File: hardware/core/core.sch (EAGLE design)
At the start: 710 parts, among them IC1 MAX481CSA, IC10 MAX481CSA, IC11 MAX481CSA, IC12 MAX481CSA, IC13 MAX481CSA, IC14 MAX481CSA, IC15 MAX481CSA, IC16 MAX481CSA, IC17 MAX481CSA, IC18 MAX481CSA, IC19 MAX481CSA, IC2 LD117AS12TR, IC20 MAX481CSA, IC21 MAX481CSA, IC22 LD117AS12TR, IC3 MAX481CSA, IC4 MAX481CSA, IC5 MAX481CSA, IC6 MAX481CSA, IC7 MAX481CSA, IC8 MAX481CSA, IC9 MAX481CSA, U1 6N138SDM

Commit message: v04 complete
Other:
- note added: "MIDI-IN Interface"
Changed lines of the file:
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@@
 <wire x1="1366.52" y1="0" x2="1366.52" y2="408.94" width="0.1524" layer="98"/>
 <wire x1="1366.52" y1="408.94" x2="254" y2="408.94" width="0.1524" layer="98"/>
+<text x="5.08" y="393.7" size="2.54" layer="98">MIDI-IN Interface</text>
 </plain>
 <instances>

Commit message: updates
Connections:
- removed net N$84: D1.C, D50.C, D51.C, D52.C, D53.C, D54.C, D55.C, D56.C
- net GND: now also D1.C, D50.C, D51.C, D52.C, D53.C, D54.C, D55.C, D56.C
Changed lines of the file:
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@@
 </part>
 <part name="GND49" library="supply1" library_urn="urn:adsk.eagle:library:371" deviceset="GND" device=""/>
-<part name="GND122" library="supply1" library_urn="urn:adsk.eagle:library:371" deviceset="GND" device=""/>
 <part name="D171" library="SMBJ8.0CA" library_urn="urn:adsk.eagle:library:39221370" deviceset="SMBJ8.0CA" device="" package3d_urn="urn:adsk.eagle:package:39221373/1">
 <attribute name="DESCRIPTION" value="600 Watt TVS 5.0v working, 9v clamp"/>
@@
 <part name="GND108" library="supply1" library_urn="urn:adsk.eagle:library:371" deviceset="GND" device=""/>
 <part name="J1" library="SparkFun-Connectors" library_urn="urn:adsk.eagle:library:513" deviceset="CONN_05X2" device="SHD" package3d_urn="urn:adsk.eagle:package:38000/1"/>
+<part name="GND122" library="supply1" library_urn="urn:adsk.eagle:library:371" deviceset="GND" device=""/>
 </parts>
 <sheets>
@@
 <attribute name="VALUE" x="949.96" y="279.4" size="1.778" layer="96"/>
 </instance>
-<instance part="GND122" gate="1" x="995.68" y="284.48" smashed="yes">
-<attribute name="VALUE" x="993.14" y="281.94" size="1.778" layer="96"/>
-</instance>
 <instance part="D171" gate="G$1" x="363.22" y="88.9" smashed="yes" rot="R90">
 <attribute name="NAME" x="363.22" y="96.52" size="1.778" layer="95" rot="R90"/>
@@
 <attribute name="NAME" x="151.13" y="122.428" size="1.778" layer="95" font="vector"/>
 </instance>
+<instance part="GND122" gate="1" x="995.68" y="281.94" smashed="yes">
+<attribute name="VALUE" x="993.14" y="279.4" size="1.778" layer="96"/>
+</instance>
 </instances>
 <busses>
@@
 <label x="165.1" y="109.22" size="1.778" layer="95"/>
 </segment>
+<segment>
+<pinref part="D56" gate="G$1" pin="C"/>
+<wire x1="995.68" y1="386.08" x2="995.68" y2="378.46" width="0.1524" layer="91"/>
+<wire x1="995.68" y1="378.46" x2="995.68" y2="370.84" width="0.1524" layer="91"/>
+<wire x1="995.68" y1="370.84" x2="995.68" y2="363.22" width="0.1524" layer="91"/>
+<wire x1="995.68" y1="363.22" x2="995.68" y2="314.96" width="0.1524" layer="91"/>
+<wire x1="995.68" y1="314.96" x2="995.68" y2="307.34" width="0.1524" layer="91"/>
+<wire x1="995.68" y1="307.34" x2="995.68" y2="299.72" width="0.1524" layer="91"/>
+<wire x1="995.68" y1="299.72" x2="995.68" y2="292.1" width="0.1524" layer="91"/>
+<wire x1="993.14" y1="292.1" x2="995.68" y2="292.1" width="0.1524" layer="91"/>
+<wire x1="995.68" y1="292.1" x2="995.68" y2="284.48" width="0.1524" layer="91"/>
+<pinref part="D55" gate="G$1" pin="C"/>
+<wire x1="993.14" y1="299.72" x2="995.68" y2="299.72" width="0.1524" layer="91"/>
+<junction x="995.68" y="299.72"/>
+<pinref part="D54" gate="G$1" pin="C"/>
+<wire x1="993.14" y1="307.34" x2="995.68" y2="307.34" width="0.1524" layer="91"/>
+<junction x="995.68" y="307.34"/>
+<pinref part="D53" gate="G$1" pin="C"/>
+<wire x1="993.14" y1="314.96" x2="995.68" y2="314.96" width="0.1524" layer="91"/>
+<junction x="995.68" y="314.96"/>
+<pinref part="D1" gate="G$1" pin="C"/>
+<wire x1="993.14" y1="386.08" x2="995.68" y2="386.08" width="0.1524" layer="91"/>
+<pinref part="D50" gate="G$1" pin="C"/>
+<wire x1="993.14" y1="378.46" x2="995.68" y2="378.46" width="0.1524" layer="91"/>
+<junction x="995.68" y="378.46"/>
+<pinref part="D51" gate="G$1" pin="C"/>
+<wire x1="993.14" y1="370.84" x2="995.68" y2="370.84" width="0.1524" layer="91"/>
+<junction x="995.68" y="370.84"/>
+<pinref part="D52" gate="G$1" pin="C"/>
+<wire x1="993.14" y1="363.22" x2="995.68" y2="363.22" width="0.1524" layer="91"/>
+<junction x="995.68" y="363.22"/>
+<pinref part="GND122" gate="1" pin="GND"/>
+</segment>
 </net>
 <net name="N$1" class="0">
@@
 </segment>
 </net>
-<net name="N$84" class="3">
-<segment>
-<pinref part="D56" gate="G$1" pin="C"/>
-<pinref part="GND122" gate="1" pin="GND"/>
-<wire x1="995.68" y1="386.08" x2="995.68" y2="378.46" width="0.1524" layer="91"/>
-<wire x1="995.68" y1="378.46" x2="995.68" y2="370.84" width="0.1524" layer="91"/>
-<wire x1="995.68" y1="370.84" x2="995.68" y2="363.22" width="0.1524" layer="91"/>
-<wire x1="995.68" y1="363.22" x2="995.68" y2="314.96" width="0.1524" layer="91"/>
-<wire x1="995.68" y1="314.96" x2="995.68" y2="307.34" width="0.1524" layer="91"/>
-<wire x1="995.68" y1="307.34" x2="995.68" y2="299.72" width="0.1524" layer="91"/>
-<wire x1="995.68" y1="299.72" x2="995.68" y2="292.1" width="0.1524" layer="91"/>
-<wire x1="993.14" y1="292.1" x2="995.68" y2="292.1" width="0.1524" layer="91"/>
-<wire x1="995.68" y1="292.1" x2="995.68" y2="287.02" width="0.1524" layer="91"/>
-<pinref part="D55" gate="G$1" pin="C"/>
-<wire x1="993.14" y1="299.72" x2="995.68" y2="299.72" width="0.1524" layer="91"/>
-<junction x="995.68" y="299.72"/>
-<pinref part="D54" gate="G$1" pin="C"/>
-<wire x1="993.14" y1="307.34" x2="995.68" y2="307.34" width="0.1524" layer="91"/>
-<junction x="995.68" y="307.34"/>
-<pinref part="D53" gate="G$1" pin="C"/>
-<wire x1="993.14" y1="314.96" x2="995.68" y2="314.96" width="0.1524" layer="91"/>
-<junction x="995.68" y="314.96"/>
-<pinref part="D1" gate="G$1" pin="C"/>
-<wire x1="993.14" y1="386.08" x2="995.68" y2="386.08" width="0.1524" layer="91"/>
-<pinref part="D50" gate="G$1" pin="C"/>
-<wire x1="993.14" y1="378.46" x2="995.68" y2="378.46" width="0.1524" layer="91"/>
-<junction x="995.68" y="378.46"/>
-<pinref part="D51" gate="G$1" pin="C"/>
-<wire x1="993.14" y1="370.84" x2="995.68" y2="370.84" width="0.1524" layer="91"/>
-<junction x="995.68" y="370.84"/>
-<pinref part="D52" gate="G$1" pin="C"/>
-<wire x1="993.14" y1="363.22" x2="995.68" y2="363.22" width="0.1524" layer="91"/>
-<junction x="995.68" y="363.22"/>
-</segment>
-</net>

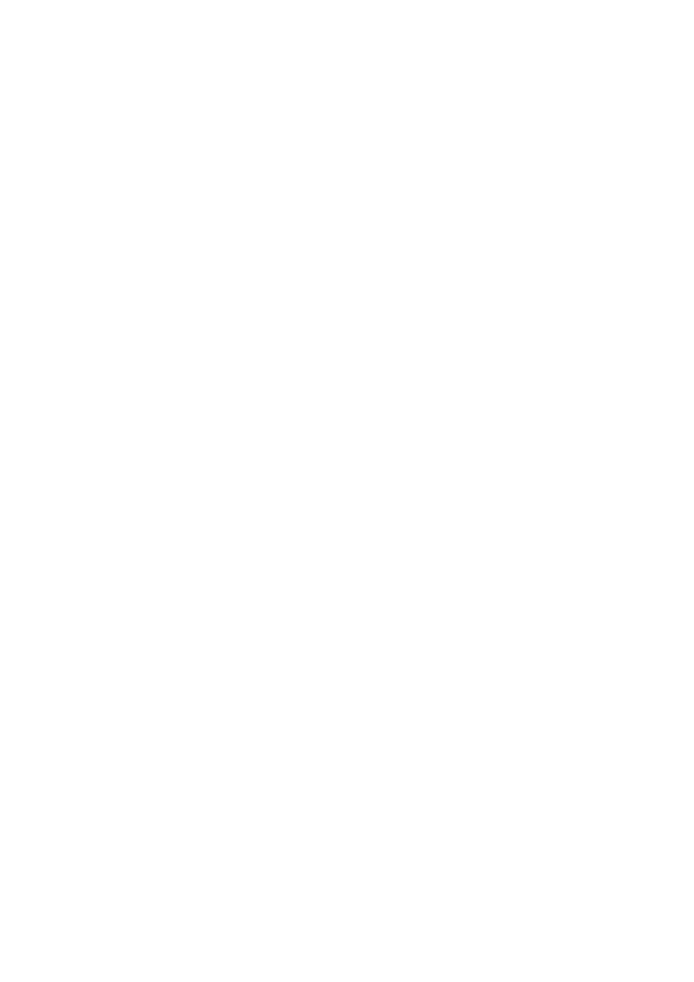
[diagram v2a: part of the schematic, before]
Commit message: add esp32-s3
(for future use)
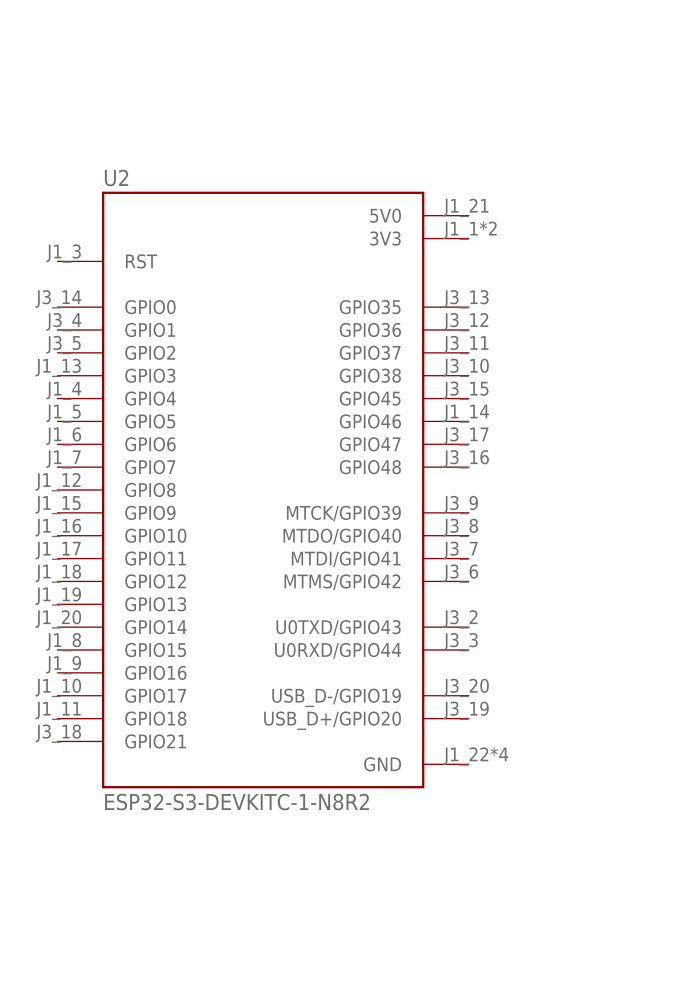
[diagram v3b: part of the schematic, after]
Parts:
- added U2: ESP32-S3-DEVKITC-1-N8R2, ESP32-S3-DEVKITC-1-N8R2:ESP32-S3-DEVKITC-1-N8R2
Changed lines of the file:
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@@
 <part name="J1" library="SparkFun-Connectors" library_urn="urn:adsk.eagle:library:513" deviceset="CONN_05X2" device="SHD" package3d_urn="urn:adsk.eagle:package:38000/1"/>
 <part name="GND122" library="supply1" library_urn="urn:adsk.eagle:library:371" deviceset="GND" device=""/>
+<part name="U2" library="ESP32-S3-DEVKITC-1-N8R2" library_urn="urn:adsk.eagle:library:40286648" deviceset="ESP32-S3-DEVKITC-1-N8R2" device="" package3d_urn="urn:adsk.eagle:package:40286651/1"/>
 </parts>
 <sheets>
@@
 <attribute name="VALUE" x="993.14" y="279.4" size="1.778" layer="96"/>
 </instance>
+<instance part="U2" gate="G$1" x="-43.18" y="190.5" smashed="yes">
+<attribute name="NAME" x="-60.96" y="226.06" size="1.778" layer="95" align="top-left"/>
+<attribute name="VALUE" x="-60.96" y="154.94" size="1.778" layer="96"/>
+</instance>
 </instances>

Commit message: re & de status LEDs added
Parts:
- removed C72: 2200uf, rcl:CPOL-USE5-13
- removed U2: ESP32-S3-DEVKITC-1-N8R2, ESP32-S3-DEVKITC-1-N8R2:ESP32-S3-DEVKITC-1-N8R2
- added D199, D200, D201, D202, D203, D204, D205, D206, D207, D208, D209, D210, D211, D212, D213, D214, D215, D216, D217, D218, D219, D220, D221, D222, D223, D224, D225, D226, D227, D228, D229, D230, D231, D232, D233, D234, D235, D236, D237, D238: (no value), SparkFun-LED:LED0603
- added JP1: (no value), pinhead:PINHD-1X3
- added R308, R309, R311, R312, R313, R314, R315, R316, R317, R318, R319, R320, R321, R322, R323, R324, R325, R326, R327, R328, R329, R330, R331, R332, R333, R334, R335, R336, R337, R338, R339, R340, R341, R342, R343, R344, R345, R346, R347, R348: 1k, rcl:R-US_R0603
- C69, C70, C71: value 2200uf -> 470uf
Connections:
- removed net 16: IC10G$1.RO, IC11G$1.RO, IC12G$1.RO, IC13G$1.RO, IC14G$1.RO, IC15G$1.RO, IC16G$1.RO, IC17G$1.RO, IC18G$1.RO, IC19G$1.RO, IC1G$1.RO, IC20G$1.RO, IC21G$1.RO, IC3G$1.RO, IC4G$1.RO, IC5G$1.RO, IC6G$1.RO, IC7G$1.RO, IC8G$1.RO, IC9G$1.RO, U$1.IO16
- removed net 17: IC10G$1.DI, IC11G$1.DI, IC12G$1.DI, IC13G$1.DI, IC14G$1.DI, IC15G$1.DI, IC16G$1.DI, IC17G$1.DI, IC18G$1.DI, IC19G$1.DI, IC1G$1.DI, IC20G$1.DI, IC21G$1.DI, IC3G$1.DI, IC4G$1.DI, IC5G$1.DI, IC6G$1.DI, IC7G$1.DI, IC8G$1.DI, IC9G$1.DI, U$1.IO17
- new net 16/RX2: IC10G$1.RO, IC11G$1.RO, IC12G$1.RO, IC13G$1.RO, IC14G$1.RO, IC15G$1.RO, IC16G$1.RO, IC17G$1.RO, IC18G$1.RO, IC19G$1.RO, IC1G$1.RO, IC20G$1.RO, IC21G$1.RO, IC3G$1.RO, IC4G$1.RO, IC5G$1.RO, IC6G$1.RO, IC7G$1.RO, IC8G$1.RO, IC9G$1.RO, JP1.2, U$1.IO16
- new net 17/TX2: IC10G$1.DI, IC11G$1.DI, IC12G$1.DI, IC13G$1.DI, IC14G$1.DI, IC15G$1.DI, IC16G$1.DI, IC17G$1.DI, IC18G$1.DI, IC19G$1.DI, IC1G$1.DI, IC20G$1.DI, IC21G$1.DI, IC3G$1.DI, IC4G$1.DI, IC5G$1.DI, IC6G$1.DI, IC7G$1.DI, IC8G$1.DI, IC9G$1.DI, JP1.3, U$1.IO17
- new net N$350: D200.A, R309.2
- new net N$351: D201.A, R311.2
- new net N$354: D202.A, R312.2
- new net N$355: D203.A, R313.2
- new net N$356: D204.A, R314.2
- new net N$357: D205.A, R315.2
- new net N$358: D206.A, R316.2
- new net N$359: D207.A, R317.2
- new net N$360: D208.A, R318.2
- new net N$361: D209.A, R319.2
- new net N$362: D210.A, R320.2
- new net N$363: D211.A, R321.2
- new net N$364: D212.A, R322.2
- new net N$365: D213.A, R323.2
- new net N$366: D214.A, R324.2
- new net N$367: D215.A, R325.2
- new net N$368: D216.A, R326.2
- new net N$369: D217.A, R327.2
- new net N$370: D218.A, R328.2
- new net N$371: D219.A, R329.2
- new net N$372: D220.A, R330.2
- new net N$373: D221.A, R331.2
- new net N$374: D222.A, R332.2
- new net N$375: D223.A, R333.2
- new net N$376: D224.A, R334.2
- new net N$377: D225.A, R335.2
- new net N$378: D226.A, R336.2
- new net N$379: D227.A, R337.2
- new net N$380: D228.A, R338.2
- new net N$381: D229.A, R339.2
- new net N$382: D230.A, R340.2
- new net N$383: D231.A, R341.2
- new net N$384: D232.A, R342.2
- new net N$385: D233.A, R343.2
- new net N$386: D234.A, R344.2
- new net N$387: D235.A, R345.2
- new net N$388: D236.A, R346.2
- new net N$389: D237.A, R347.2
- new net N$390: D238.A, R348.2
- new net N$84: D199.A, R308.2
- net +3V3: no longer C72.+
- net F0: now also R309.1
- net F1: now also R308.1
- net F10: now also R320.1
- net F11: now also R319.1
- net F12: now also R322.1
- net F13: now also R321.1
- net F14: now also R324.1
- net F15: now also R323.1
- net F2: now also R312.1
- net F3: now also R311.1
- net F4: now also R314.1
- net F5: now also R313.1
- net F6: now also R316.1
- net F7: now also R315.1
- net F8: now also R318.1
- net F9: now also R317.1
- net G0: now also R326.1
- net G1: now also R325.1
- net G10: now also R336.1
- net G11: now also R335.1
- net G12: now also R338.1
- net G13: now also R337.1
- net G14: now also R340.1
- net G15: now also R339.1
- net G2: now also R328.1
- net G3: now also R327.1
- net G4: now also R330.1
- net G5: now also R329.1
- net G6: now also R332.1
- net G7: now also R331.1
- net G8: now also R334.1
- net G9: now also R333.1
- net GND: now also D199.C, D200.C, D201.C, D202.C, D203.C, D204.C, D205.C, D206.C, D207.C, D208.C, D209.C, D210.C, D211.C, D212.C, D213.C, D214.C, D215.C, D216.C, D217.C, D218.C, D219.C, D220.C, D221.C, D222.C, D223.C, D224.C, D225.C, D226.C, D227.C, D228.C, D229.C, D230.C, D231.C, D232.C, D233.C, D234.C, D235.C, D236.C, D237.C, D238.C, JP1.1; no longer C72.-
- net H0: now also R342.1
- net H1: now also R341.1
- net H2: now also R344.1
- net H3: now also R343.1
- net H4: now also R346.1
- net H5: now also R345.1
- net H6: now also R348.1
- net H7: now also R347.1
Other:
- moved on the sheet: APA102, D196, D197, IC10P, IC11P, IC12P, IC13P, IC14P, IC15P, IC16P, IC17P, IC18P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
